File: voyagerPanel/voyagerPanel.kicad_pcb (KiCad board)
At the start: 2 copper layers, 70 x 50 mm, 44 parts, among them J1 USB_C_Receptacle_USB2.0_16P, J2 Battery Pin, J3 E-ink, J4 BME280_MODULE, SW1 SW_Push_45deg, SW2 SW_Push_45deg, SW3 SW_Push_45deg, SW4 SW_Push_45deg, U1 ESP32-S3-MINI-1, U2 MCP1700x-330xxMB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

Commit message: PCB almost finished end of day 2
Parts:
- moved C12 112.2 mm to (32.4, 67.5), turned to 180 degrees
- moved C8 94.2 mm to (48.0, 66.0), turned to 180 degrees
- moved C7 92.2 mm to (48.0, 68.1), turned to 180 degrees
- moved I2CSCL1 86.9 mm to (38.0, 66.8)
- moved RC1 85.1 mm to (35.3, 98.9)
- moved RC2 85.1 mm to (35.3, 102.5)
- moved I2CSDA1 84.7 mm to (42.0, 66.8)
- moved C1 74.8 mm to (54.4, 101.0), turned to -90 degrees
- moved C6 72.0 mm to (64.4, 79.5), turned to 180 degrees
- moved e-ink1 70.5 mm to (56.0, 80.3), turned to -90 degrees
- moved C3 68.0 mm to (64.4, 81.6), turned to 180 degrees
- moved C11 66.6 mm to (78.5, 72.8), turned to 90 degrees
- moved RLED1 64.4 mm to (70.2, 70.8)
- moved C5 62.3 mm to (71.6, 104.3), turned to 180 degrees
- moved C2 59.7 mm to (71.5, 83.8), turned to -90 degrees
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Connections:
- BTNNEXT1 pad 1: PROG_IO0 -> +3V3
- BTNSELECT1 pad 1: PROG_IO0 -> +3V3
- C12 pad 1: PROG_IO0 -> +3V3
- C3 pad 1: PROG_IO0 -> +3V3
- C6 pad 1: PROG_IO0 -> +3V3
- C7 pad 1: PROG_IO0 -> +3V3
- C8 pad 1: PROG_IO0 -> +3V3
- EN1 pad 1: PROG_IO0 -> +3V3
- I2CSCL1 pad 1: PROG_IO0 -> +3V3
- I2CSDA1 pad 1: PROG_IO0 -> +3V3
- J3 pad 1: PROG_IO0 -> +3V3
- J4 pad 1: PROG_IO0 -> +3V3
- U1 pad 3: PROG_IO0 -> +3V3
- U2 pad 3: PROG_IO0 -> +3V3
- e-ink1 pad 2: PROG_IO0 -> +3V3
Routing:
- net +3V3: track 0.00 -> 137.5 mm, vias 0 -> 3
- net PROG_IO0: track 0.00 -> 72.9 mm, vias 0 -> 2
- net BTN_SELECT: track 0.00 -> 64.3 mm, vias 0 -> 2
- net BTN_NEXT: track 0.00 -> 58.4 mm, vias 0 -> 2
- net VBAT: track 0.00 -> 40.3 mm
- net PROG_EN: track 0.00 -> 39.0 mm
- net EPD_BUSY: track 0.00 -> 37.7 mm, vias 0 -> 1
- net EPD_DC: track 0.00 -> 35.5 mm
- net EPD_RST: track 0.00 -> 34.5 mm, vias 0 -> 1
- net EPD_SCK: track 0.00 -> 29.1 mm, vias 0 -> 1
- net EPD_CS: track 0.00 -> 28.7 mm, vias 0 -> 2
- net EPD_MOSI: track 0.00 -> 26.3 mm, vias 0 -> 1
- net +5V: track 43.9 -> 66.2 mm
- net I2C_SCL: track 0.00 -> 22.1 mm, vias 0 -> 1
- net I2C_SDA: track 0.00 -> 20.1 mm, vias 0 -> 1
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- added copper zone on B.Cu, net GND
- added copper zone on F.Cu, net GND

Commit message: finished PCB
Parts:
- added G***: LOGO, LOGO, F.Cu at (42.2, 81.5)
- moved R14 12.7 mm to (48.0, 74.5), turned to 90 degrees
- moved R15 7.35 mm to (48.0, 71.1), turned to -90 degrees
- moved C7 1.67 mm to (47.1, 66.7)
- moved C8 1.67 mm to (47.1, 64.6)
- moved C12 1.51 mm to (31.0, 67.0)
- renumbered BTNNEXT1 to R10, I2CSCL1 to R14, I2CSDA1 to R15, BTNSELECT1 to R9
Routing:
- net PROG_IO0: track 72.9 -> 54.3 mm
- net +3V3: track 137.5 -> 147.6 mm
- net PROG_EN: track 39.0 -> 35.6 mm
- net I2C_SDA: track 20.1 -> 17.4 mm
- net GND: track 0.00 -> 1.63 mm, vias 0 -> 1
- net I2C_SCL: track 22.1 -> 20.9 mm
- net +5V: track 66.2 -> 65.6 mm
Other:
- board size 70 x 50 mm -> 71 x 50.3 mm
- board text added: "By Cocotrilo & STASIS HackClub"
- board text added: "VP"
- board text added: "Voyager-Panel"

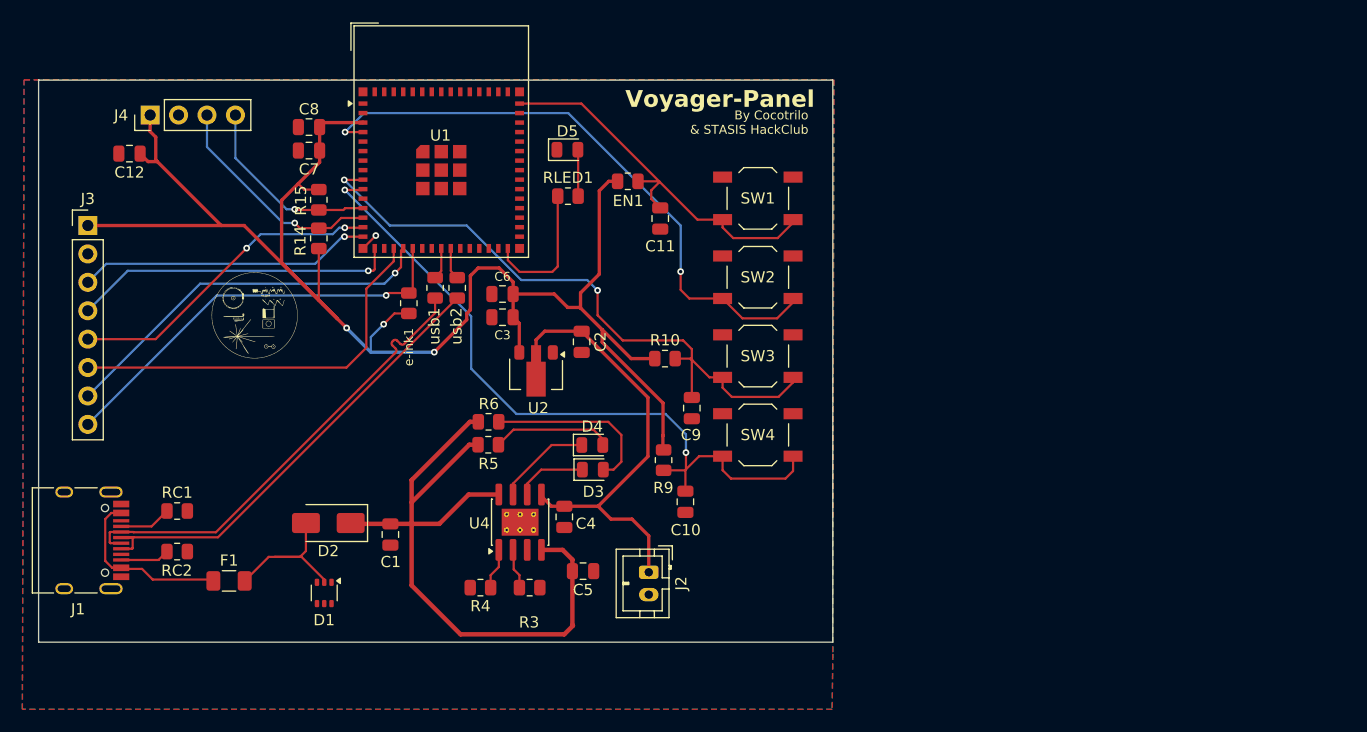
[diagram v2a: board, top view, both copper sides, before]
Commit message: Firmware finalized!
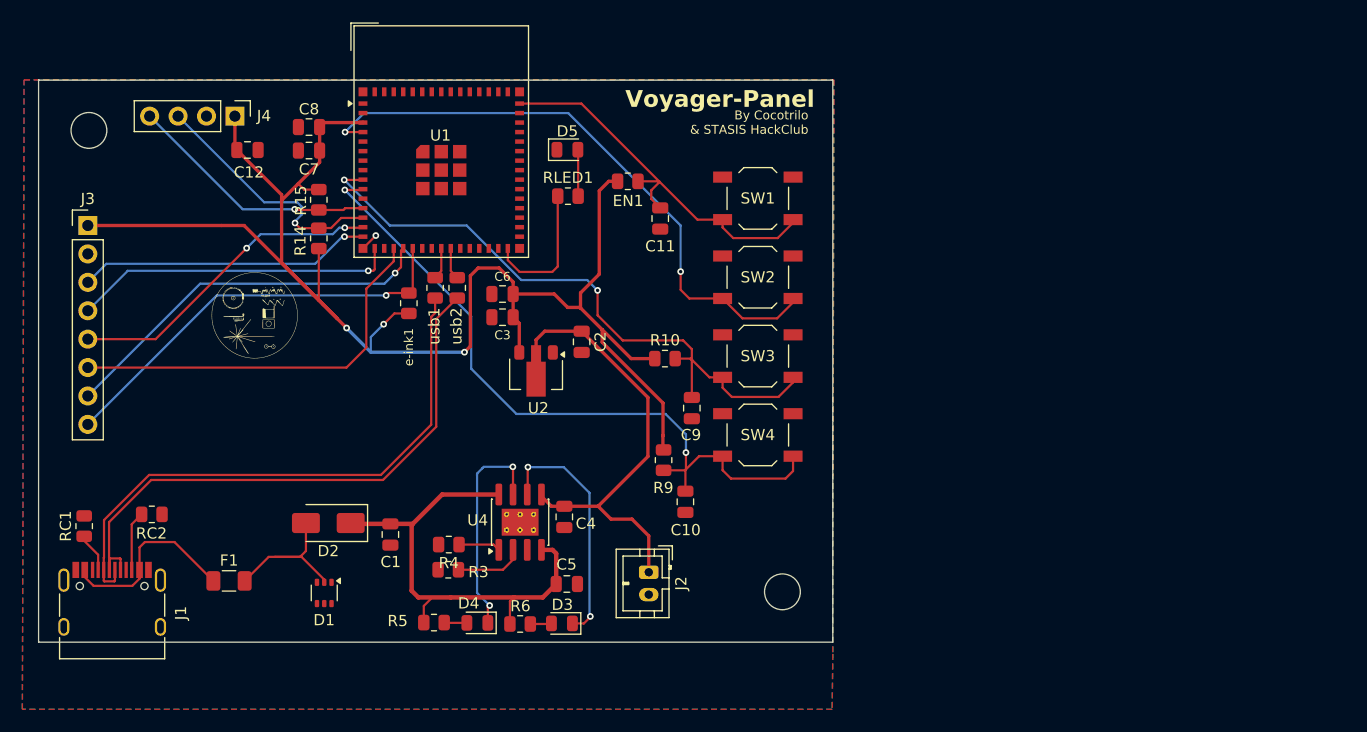
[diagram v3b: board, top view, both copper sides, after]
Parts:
- added REF**: MountingHole_3.2mm_M3, MountingHole:MountingHole_3.2mm_M3, F.Cu at (89.4, 106.2)
- added REF**: MountingHole_3.2mm_M3, MountingHole:MountingHole_3.2mm_M3, F.Cu at (27.4, 64.9)
- moved D4 18.9 mm to (62.1, 108.9), turned to 180 degrees
- moved R6 18.3 mm to (66.0, 109.0)
- moved R5 16.6 mm to (58.2, 108.9)
- moved D3 14.0 mm to (69.7, 109.0), turned to 180 degrees
- moved C12 10.6 mm to (41.6, 66.7), turned to 0 degrees
- moved RC1 8.42 mm to (27.0, 100.3), turned to 90 degrees
- moved J4 7.58 mm to (40.5, 63.6), turned to -90 degrees
- moved R3 7.45 mm to (59.5, 104.2), turned to 180 degrees
- moved J1 7.43 mm to (29.5, 108.2), turned to 0 degrees
- moved R4 4.78 mm to (59.6, 101.9)
- moved RC2 4.02 mm to (33.0, 99.2)
- moved C5 1.85 mm to (70.1, 105.5)
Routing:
- net +5V: track 65.6 -> 43.3 mm
- net Net-(D3-K): track 6.42 -> 21.9 mm, vias 0 -> 2
- net Net-(D3-A): track 15.8 -> 1.91 mm
- net Net-(D4-K): track 8.55 -> 19.8 mm, vias 0 -> 2
- net USB_D+: track 41.9 -> 52.3 mm
- net USB_D-: track 42.2 -> 52.0 mm
- net Net-(D4-A): track 10.8 -> 2.04 mm
- net I2C_SDA: track 17.4 -> 22.8 mm
- net +3V3: track 147.6 -> 144.0 mm
- net Net-(U4-PROG): track 3.61 -> 6.13 mm
- net I2C_SCL: track 20.9 -> 22.8 mm
- net Net-(J1-CC1): track 4.66 -> 3.12 mm
- net Net-(F1-Pad1): track 15.8 -> 17.3 mm
- net Net-(J1-CC2): track 4.40 -> 5.33 mm
- net GND: track 1.63 -> 2.30 mm
